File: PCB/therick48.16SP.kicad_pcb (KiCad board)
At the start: 2 copper layers, 312.4 x 75.8 mm, 173 parts, among them J1 TYPE-C-31-M12_13, J2 AVR-ISP-6_mod, K1 KEYSW, K10 KEYSW, K11 KEYSW, K12 KEYSW, K13 KEYSW, K14 KEYSW, K15 KEYSW, K16 KEYSW, K17 KEYSW, K18 KEYSW, K19 KEYSW, K2 KEYSW, K20 KEYSW, K21 KEYSW, K22 KEYSW, K23 KEYSW, K24 KEYSW, K25 KEYSW, K26 KEYSW, K27 KEYSW, K28 KEYSW, K29 KEYSW, K3 KEYSW, K30 KEYSW, K31 KEYSW, K32 KEYSW, K33 KEYSW, K34 KEYSW, K35 KEYSW, K36 KEYSW, K37 KEYSW, K38 KEYSW, K39 KEYSW, K4 KEYSW, K40 KEYSW, K41 KEYSW, K42 KEYSW, K43 KEYSW, K44 KEYSW, K45 KEYSW, K46 KEYSW, K47 KEYSW, K48 KEYSW, K49 KEYSW, K5 KEYSW, K50 KEYSW, K51 KEYSW, K52 KEYSW, K53 KEYSW, K54 KEYSW, K55 KEYSW, K56 KEYSW, K57 KEYSW, K58 KEYSW, K59 KEYSW, K6 KEYSW, K60 KEYSW, K61 KEYSW, K62 KEYSW, K63 KEYSW, K64 KEYSW, K7 KEYSW, K8 KEYSW, K9 KEYSW, SW1 SW_PUSH, U1 ATMEGA32U4, U2 HOLE, U3 USBLC6-2SC6, U4 HOLE, U5 HOLE, U6 HOLE, U7 HOLE, U8 HOLE, Y1 16MHz

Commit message: Changed gap between 4X12 and 4X4 to .25 inches
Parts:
- moved H8 3.42 mm to (109.8, 61.9)
- moved K49 3.42 mm to (62.3, 52.4)
- moved K53 3.42 mm to (62.3, 71.4)
- moved K57 3.42 mm to (62.3, 90.4)
- moved K61 3.42 mm to (62.3, 109.4)
- moved D49 3.42 mm to (70.3, 50.7)
- moved D50 3.42 mm to (73.3, 50.7)
- moved D51 3.42 mm to (108.3, 50.7)
- moved D52 3.42 mm to (111.3, 50.7)
- moved D53 3.42 mm to (70.3, 69.8)
- moved D54 3.42 mm to (73.3, 69.8)
- moved D55 3.42 mm to (108.3, 69.8)
- moved D56 3.42 mm to (111.3, 69.8)
- moved D57 3.42 mm to (70.3, 88.8)
- moved D58 3.42 mm to (73.3, 88.8)
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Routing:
- net row3: track 324.7 -> 321.3 mm
- net col14: track 175.7 -> 172.3 mm
- net row1: track 296.4 -> 292.9 mm
- net col13: track 159.6 -> 156.2 mm
- net row2: track 342.5 -> 339.1 mm
- net row0: track 342.6 -> 339.2 mm
- net col12: track 178.2 -> 174.8 mm
- net col15: track 121.1 -> 117.7 mm
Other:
- board size 312.4 x 75.8 mm -> 308.9 x 75.8 mm

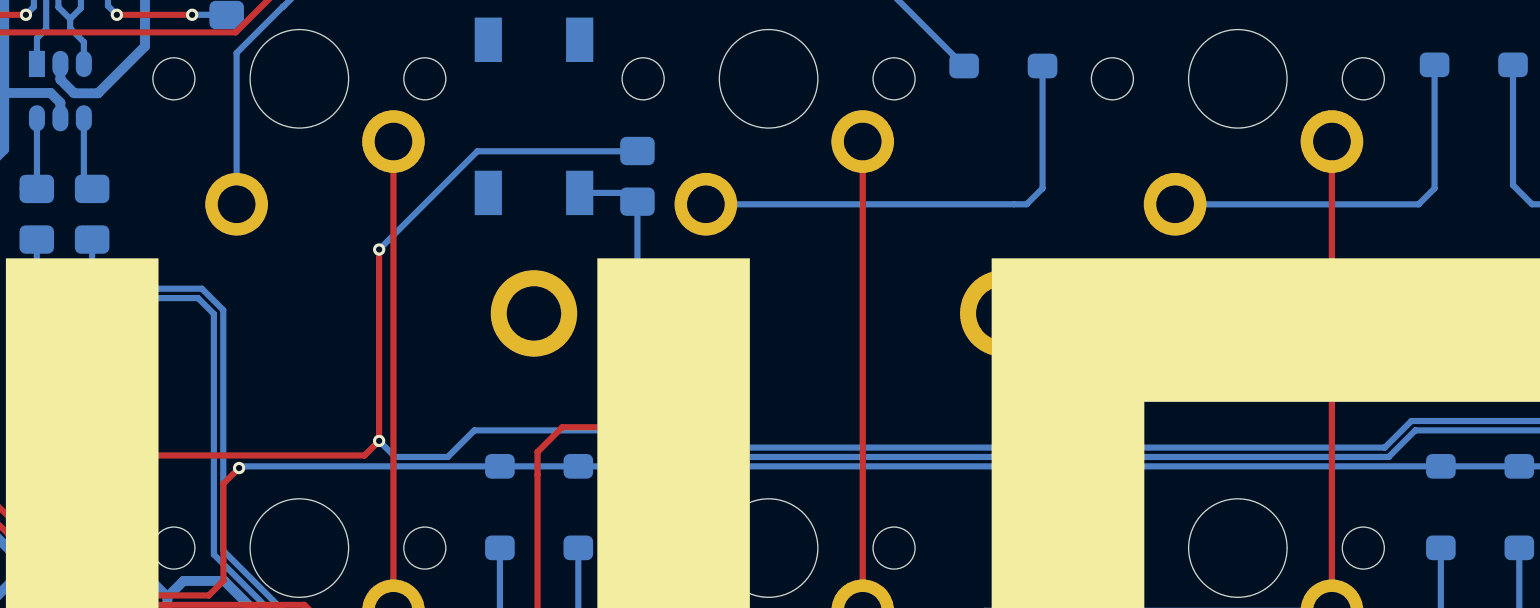
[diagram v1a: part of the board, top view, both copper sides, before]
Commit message: Changed a trace
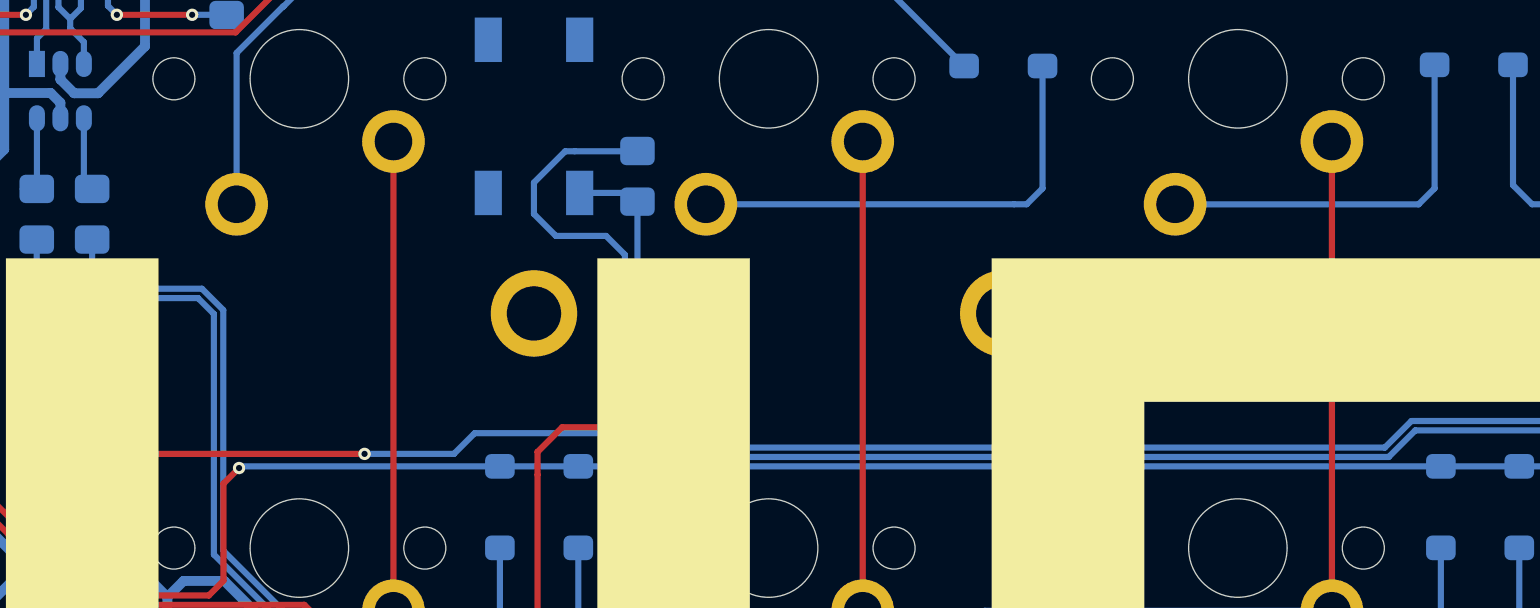
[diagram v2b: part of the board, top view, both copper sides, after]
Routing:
- net VCC: track 216.9 -> 214.0 mm, vias 7 -> 6
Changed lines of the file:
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@@
     (thickness 1.6)
     (drawings 81)
-    (tracks 811)
+    (tracks 814)
     (zones 0)
     (modules 173)
@@
   (segment (start 165.588002 78.886998) (end 165.588002 85.705002) (width 0.4) (layer F.Cu) (net 49))
   (segment (start 170.053 75.057) (end 169.418001 75.057) (width 0.4) (layer F.Cu) (net 49))
-  (via (at 186.010499 59.351502) (size 0.5) (drill 0.25) (layers F.Cu B.Cu) (net 49))
-  (segment (start 189.988249 55.373752) (end 196.773749 55.373752) (width 0.25) (layer B.Cu) (net 49))
-  (segment (start 186.010499 59.351502) (end 189.988249 55.373752) (width 0.25) (layer B.Cu) (net 49))
   (segment (start 174.650499 72.199002) (end 176.212002 72.199002) (width 0.4) (layer B.Cu) (net 49))
   (segment (start 177.437499 73.424499) (end 177.437499 76.605002) (width 0.4) (layer B.Cu) (net 49))
@@
   (segment (start 178.090998 72.771) (end 179.744227 72.771) (width 0.4) (layer B.Cu) (net 49))
   (segment (start 177.437499 73.424499) (end 178.090998 72.771) (width 0.4) (layer B.Cu) (net 49))
-  (segment (start 176.212002 72.199002) (end 176.212002 68.262998) (width 0.25) (layer B.Cu) (net 49))
-  (segment (start 176.784 67.691) (end 176.212002 68.262998) (width 0.25) (layer F.Cu) (net 49))
-  (segment (start 186.010499 67.100501) (end 185.42 67.691) (width 0.25) (layer F.Cu) (net 49))
-  (segment (start 186.010499 59.351502) (end 186.010499 67.100501) (width 0.25) (layer F.Cu) (net 49))
-  (segment (start 185.42 67.691) (end 176.784 67.691) (width 0.25) (layer F.Cu) (net 49))
-  (via (at 176.212002 68.262998) (size 0.5) (drill 0.25) (layers F.Cu B.Cu) (net 49))
   (segment (start 249.3064 57.88) (end 250.92 57.88) (width 0.25) (layer B.Cu) (net 49))
   (segment (start 250.92 57.88) (end 251.206 58.166) (width 0.25) (layer B.Cu) (net 49))
@@
   (segment (start 233.299 66.675) (end 227.965 66.675) (width 0.25) (layer B.Cu) (net 49))
   (segment (start 227.965 66.675) (end 226.888633 67.751367) (width 0.25) (layer B.Cu) (net 49))
-  (segment (start 226.888633 67.751367) (end 196.275367 67.751367) (width 0.25) (layer B.Cu) (net 49))
-  (segment (start 196.275367 67.751367) (end 195.199 66.675) (width 0.25) (layer B.Cu) (net 49))
-  (segment (start 195.199 66.675) (end 189.865 66.675) (width 0.25) (layer B.Cu) (net 49))
-  (segment (start 189.865 66.675) (end 188.788633 67.751367) (width 0.25) (layer B.Cu) (net 49))
-  (segment (start 186.661365 67.751367) (end 186.010499 67.100501) (width 0.25) (layer B.Cu) (net 49))
-  (via (at 186.010499 67.100501) (size 0.5) (drill 0.25) (layers F.Cu B.Cu) (net 49))
-  (segment (start 188.788633 67.751367) (end 186.661365 67.751367) (width 0.25) (layer B.Cu) (net 49))
+  (segment (start 193.930752 55.373752) (end 193.546248 55.373752) (width 0.25) (layer B.Cu) (net 49))
+  (segment (start 193.930752 55.373752) (end 196.773749 55.373752) (width 0.25) (layer B.Cu) (net 49))
+  (segment (start 193.546248 55.373752) (end 192.278 56.642) (width 0.25) (layer B.Cu) (net 49))
+  (segment (start 192.278 56.642) (end 192.278 57.912) (width 0.25) (layer B.Cu) (net 49))
+  (segment (start 192.278 57.912) (end 193.167 58.801) (width 0.25) (layer B.Cu) (net 49))
+  (segment (start 193.167 58.801) (end 195.199 58.801) (width 0.25) (layer B.Cu) (net 49))
+  (segment (start 195.199 58.801) (end 195.961 59.563) (width 0.25) (layer B.Cu) (net 49))
+  (segment (start 195.961 59.563) (end 195.961 66.787402) (width 0.25) (layer B.Cu) (net 49))
+  (segment (start 195.961 66.787402) (end 189.879598 66.787402) (width 0.25) (layer B.Cu) (net 49))
+  (segment (start 189.040623 67.626377) (end 185.42 67.626377) (width 0.25) (layer B.Cu) (net 49))
+  (segment (start 189.879598 66.787402) (end 189.040623 67.626377) (width 0.25) (layer B.Cu) (net 49))
+  (via (at 185.42 67.626377) (size 0.5) (drill 0.25) (layers F.Cu B.Cu) (net 49))
+  (segment (start 176.212002 72.199002) (end 176.212002 68.262998) (width 0.25) (layer B.Cu) (net 49))
+  (segment (start 176.784 67.691) (end 176.212002 68.262998) (width 0.25) (layer F.Cu) (net 49))
+  (via (at 176.212002 68.262998) (size 0.5) (drill 0.25) (layers F.Cu B.Cu) (net 49))
+  (segment (start 176.848623 67.626377) (end 176.784 67.691) (width 0.25) (layer F.Cu) (net 49))
+  (segment (start 185.42 67.626377) (end 176.848623 67.626377) (width 0.25) (layer F.Cu) (net 49))
+  (segment (start 196.924965 67.751367) (end 226.888633 67.751367) (width 0.25) (layer B.Cu) (net 49))
+  (segment (start 195.961 66.787402) (end 196.924965 67.751367) (width 0.25) (layer B.Cu) (net 49))
   (segment (start 181.118393 80.905002) (end 179.337499 80.905002) (width 0.25) (layer B.Cu) (net 50))
   (segment (start 182.99978 79.023617) (end 181.118393 80.905002) (width 0.25) (layer B.Cu) (net 50))

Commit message: 48+16SP to 48.16SP
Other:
- board text added: "therick48.16SP"
- board text removed: "therick48+16SP"
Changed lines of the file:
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@@
     (arrow2b (pts (xy 128.844686 37.9999) (xy 129.97119 37.413479)))
   )
-  (gr_text therick48+16SP (at 170.307 116.459) (layer B.SilkS)
+  (gr_text therick48.16SP (at 170.688 116.459) (layer B.SilkS)
     (effects (font (size 1.25 1.25) (thickness 0.2)) (justify mirror))
   )
